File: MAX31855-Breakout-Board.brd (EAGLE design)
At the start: 15.2 x 15.2 mm, 5 parts, among them U1 MAX6675MAX31855

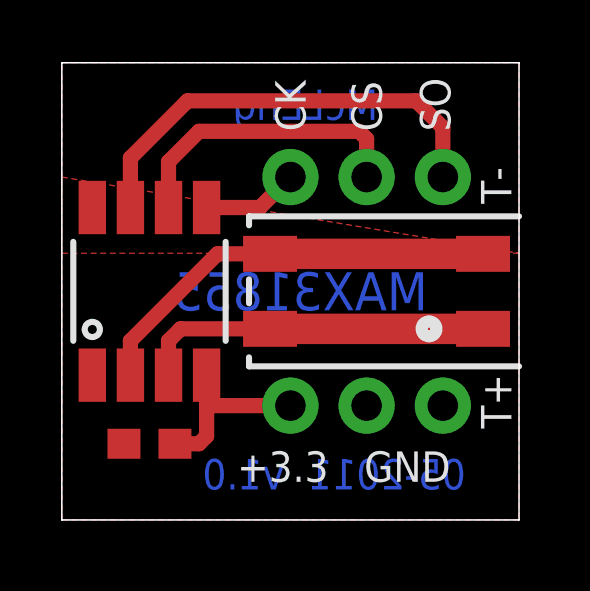
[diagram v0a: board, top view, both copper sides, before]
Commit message: Updated to use screw terminal header and updated for v1.1 and 01-2012 production
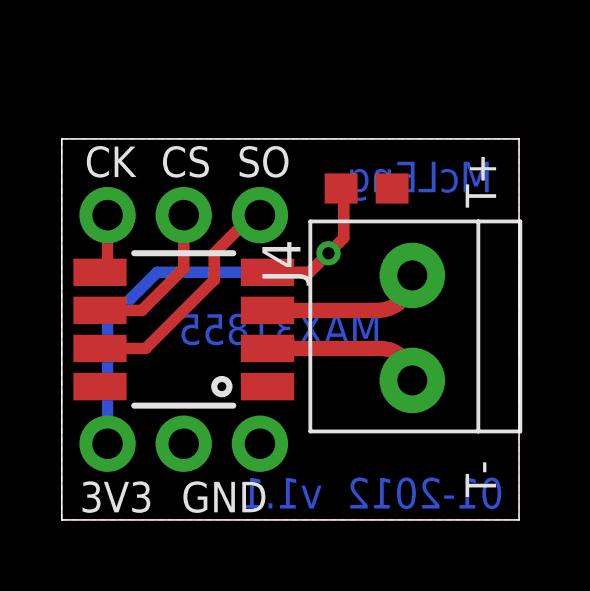
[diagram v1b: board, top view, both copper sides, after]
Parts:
- removed J1: (no value), McLEng:WIRE-TO-BOARD_SMD_2WAY
- added J4: 1X2-3.5MM, adafruit:1X2-3.5MM
- moved C1 11.2 mm to (10.2, 11.0), turned to 0 degrees
- moved J3 6.23 mm to (1.52, 2.54)
- moved J2 6.23 mm to (6.60, 10.2)
- moved U1 1.71 mm to (4.06, 6.35), turned to 180 degrees
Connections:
- removed net N$1: J1.P2-1, J1.P2-2, U1.T-
- removed net N$2: J1.P1-1, J1.P1-2, U1.T+
- new net T+: J4.1, U1.T+
- new net T-: J4.2, U1.T-
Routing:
- net N$1: track 14.1 -> 0.00 mm
- net N$2: track 11.8 -> 0.00 mm
- net +5V: track 5.99 -> 17.6 mm, vias 0 -> 1
- net SO: track 14.9 -> 7.70 mm
- net T+: track 0.00 -> 5.31 mm
- net T-: track 0.00 -> 5.27 mm
- net CS: track 9.92 -> 5.15 mm
- net SCK: track 3.21 -> 2.01 mm
- removed copper zone on layer 1, net N$3
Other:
- board size 15.2 x 15.2 mm -> 15.2 x 12.7 mm
- board text added: "01-2012 v1.1"
- board text added: "3V3"
- board text removed: "+3.3"
- board text removed: "05-2011 v1.0"
